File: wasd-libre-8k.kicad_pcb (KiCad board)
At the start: 2 copper layers, 100 x 39 mm, 72 parts, among them J1 Conn_01x05, J12 Conn_01x05, J2 USB_C_Receptacle_USB2.0, J3 Conn_01x07, J32 Conn_01x30, U1 MX25R3235FM1xx1, U2 ICE40HX1K-TQ144, U20 ICE40HX8K-BG121, U3 NCV8114ASN120T1G, U4 NCV8114ASN330T1G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

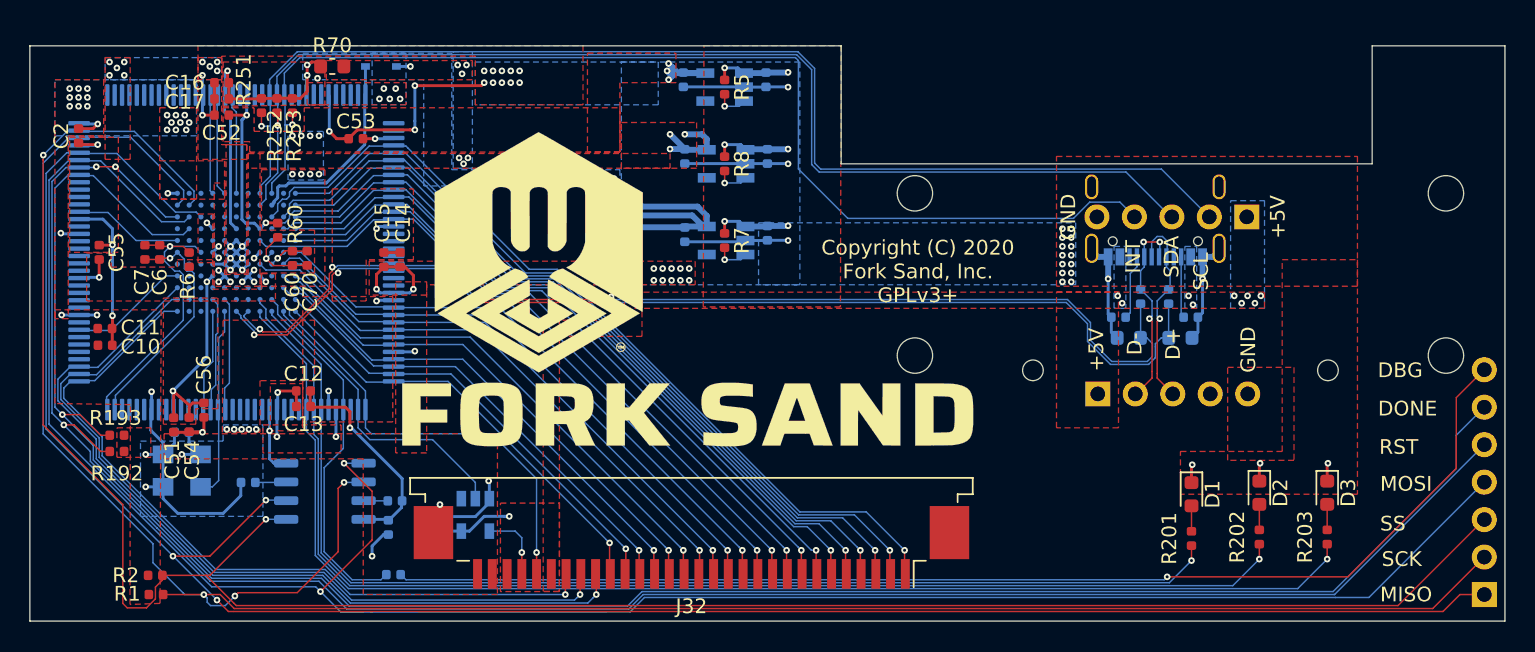
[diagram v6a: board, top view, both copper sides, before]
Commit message: Reworked for production cost decrease
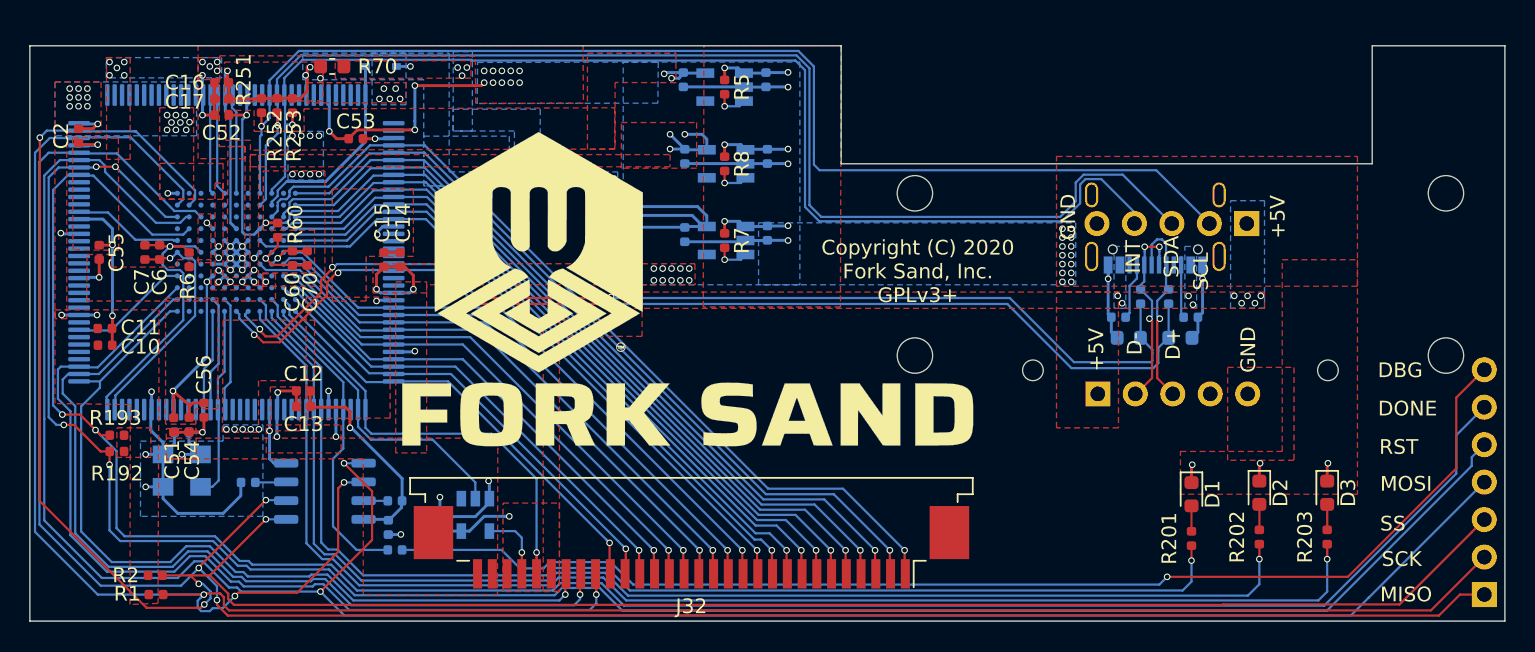
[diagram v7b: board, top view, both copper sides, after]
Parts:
- moved R120 1.68 mm to (84.8, 94.2)
- moved J2 0.55 mm to (136.3, 72.3)
- moved J1 0.45 mm to (142.5, 72.0)
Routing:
- net /COL5: track 56.0 -> 62.9 mm
- net /ICE_MOSI: track 147.0 -> 153.5 mm
- net /ICE_SCK: track 156.1 -> 162.5 mm
- net /COL6: track 54.2 -> 60.3 mm
- net /ICE_MISO: track 142.6 -> 148.3 mm
- net /COL7: track 51.5 -> 56.6 mm
- net /I2C0_SDA: track 79.5 -> 84.3 mm
- net /ICE_SS: track 150.4 -> 155.0 mm, vias 2 -> 4
- net GND: track 123.5 -> 119.1 mm
- net /INTERRUPT: track 77.5 -> 81.1 mm
- net +1V2: track 41.9 -> 38.3 mm, vias 19 -> 18
- net /DEBUG: track 24.7 -> 22.0 mm
- net /DEBUG_LED3: track 89.5 -> 91.7 mm
- net /DEBUG_LED2: track 85.5 -> 87.2 mm
- net /DEBUG_LED1: track 79.3 -> 80.8 mm
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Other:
- net class BigPower: via_drill 0.2 -> 0.3
- net class Default: clearance 0.1 -> 0.148; trace_width 0.1 -> 0.1524; via_drill 0.2 -> 0.3
- net class Power: via_drill 0.2 -> 0.3
- rule trace_clearance: 0.1 -> 0.148
- rule trace_min: 0.1 -> 0.1524
- rule via_min_size: 0.4 -> 0.45
